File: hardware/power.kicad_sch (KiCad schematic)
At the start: 35 parts

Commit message: finish power tree
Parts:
- removed C? (x3): 100n, symbol Device:C_Small
- removed C?: 1u, symbol Device:C_Small
- removed Q? (x6): CSD18540Q5B, Package_TO_SOT_SMD:TDSON-8-1, symbol Transistor_FET:CSD18540Q5B
- removed R?: 250k, symbol Device:R_Small
- removed U? (x3): LM5109BSD, Package_SON:WSON-8-1EP_4x4mm_P0.8mm_EP2.6x3mm, symbol Driver_FET:LM5109BSD
- removed U?: TPS76733, Package_SO:SOIC-8_3.9x4.9mm_P1.27mm, symbol Regulator_Linear:TPS76733
- added C? (x2): 1u, symbol Device:C_Small
- added C? (x2): 22u, symbol Device:C_Small
- added C?: 100n, symbol Device:C_Small
- added D?: SS34, Diode_THT:D_DO-35_SOD27_P7.62mm_Horizontal, symbol Diode:1N4148
- added L?: 22u, symbol Device:L_Small
- added R?: 150k, symbol Device:R_Small
- added R?: 10k, symbol Device:R_Small
- added U?: MT3608, Package_TO_SOT_SMD:SOT-23-6, symbol Regulator_Switching:MT3608
- added U?: AMS1117-3.3, Package_TO_SOT_SMD:SOT-223-3_TabPin2, symbol Regulator_Linear:AMS1117-3.3
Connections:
- net +3V3: now also C?.1, U?.2 (VO)
- net +5V: now also C?.1, C?.1, L?.1, U?.3 (VI), U?.4 (EN), U?.5 (IN)
- net GND: now also C?.2, C?.2, C?.2, C?.2, C?.2, R?.2, U?.1 (GND), U?.2 (GND), U?.3 (FB)
- new net: D?.1 (K), L?.2, U?.1 (SW)
- new net: R?.1, R?.2
- new net +10V: C?.1, C?.1, D?.2 (A), R?.1
- no-connect marks 1 -> 0
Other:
- note added: "vout = 0.6v * (150k/10k) = 9.6v"
- note removed: "3 phase half bridge"
- moved on the sheet: C?, L?, R?, U?

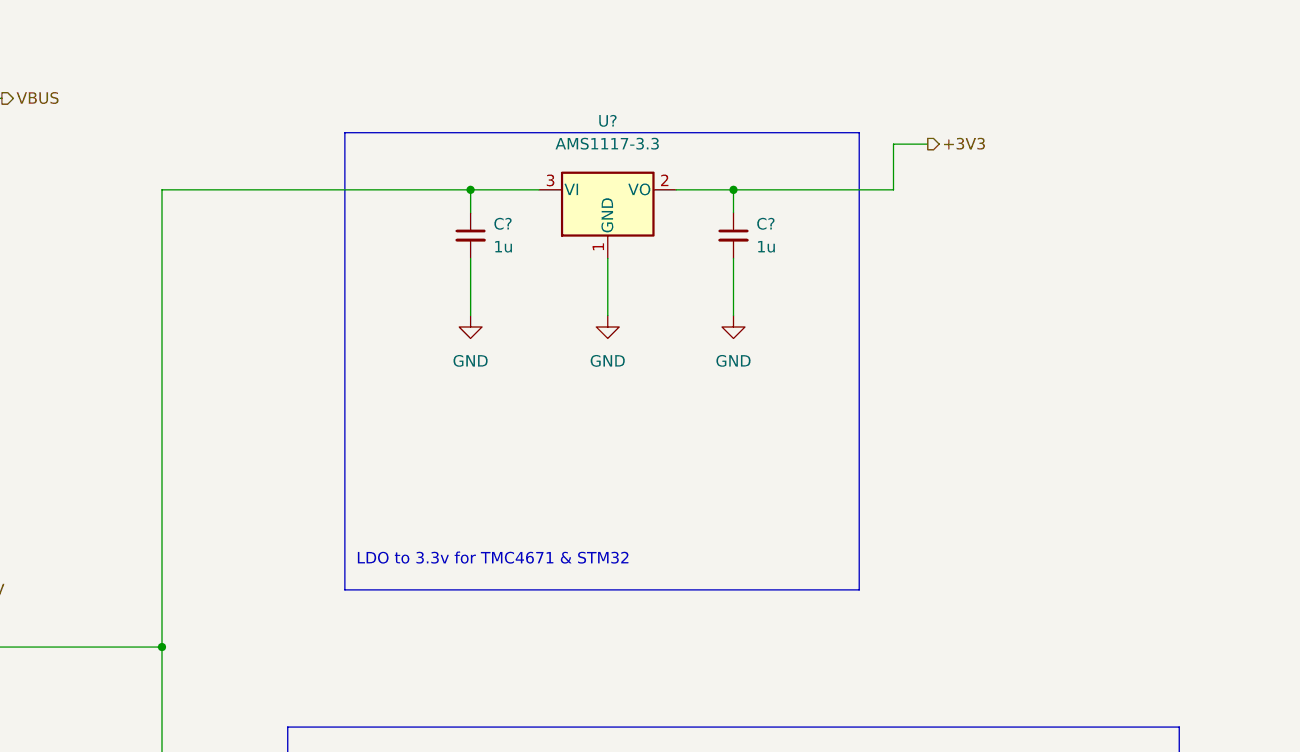
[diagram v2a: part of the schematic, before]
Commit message: add 1.8v LDO for TMC4671 core
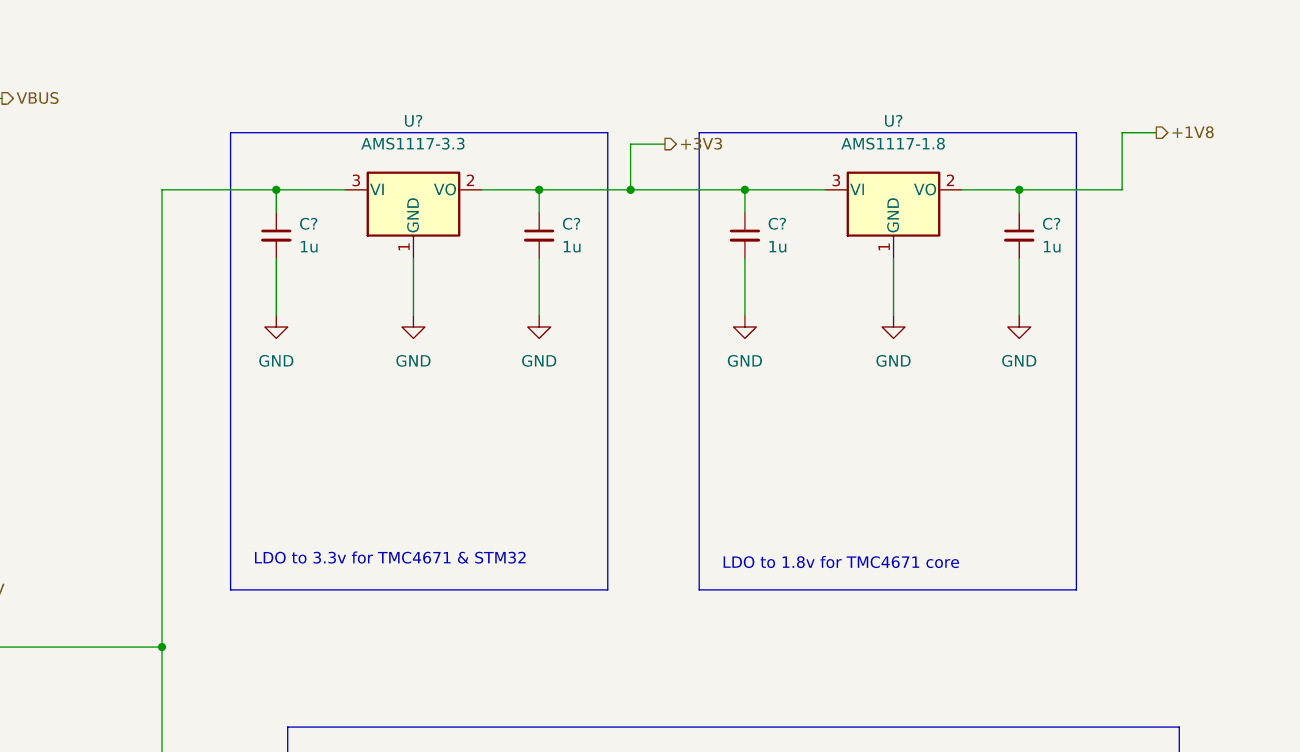
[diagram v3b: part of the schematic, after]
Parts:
- added C? (x2): 1u, symbol Device:C_Small
- added U?: AMS1117-1.8, Package_TO_SOT_SMD:SOT-223-3_TabPin2, symbol Regulator_Linear:AMS1117-1.8
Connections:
- net +3V3: now also C?.1, U?.3 (VI)
- net GND: now also C?.2, C?.2, U?.1 (GND)
- new net +1V8: C?.1, U?.2 (VO)
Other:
- note added: "LDO to 1.8v for TMC4671 core"
- moved on the sheet: C?, U?

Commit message: add firmware
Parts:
- C12, C13, C14, C15, C16, C17, C18, C19, C20, C21, C22, C23, C24, C25, C26, C27, C28, C29: renamed from C?; footprint (none) -> Capacitor_SMD:C_0402_1005Metric
- D1: renamed from D?; footprint Diode_THT:D_DO-35_SOD27_P7.62mm_Horizontal -> (none)
- gave numbers to parts that had none: 15
